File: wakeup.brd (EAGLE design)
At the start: 100 x 80 mm, 14 parts, among them IC2 ATMEGA48/88/168-AU

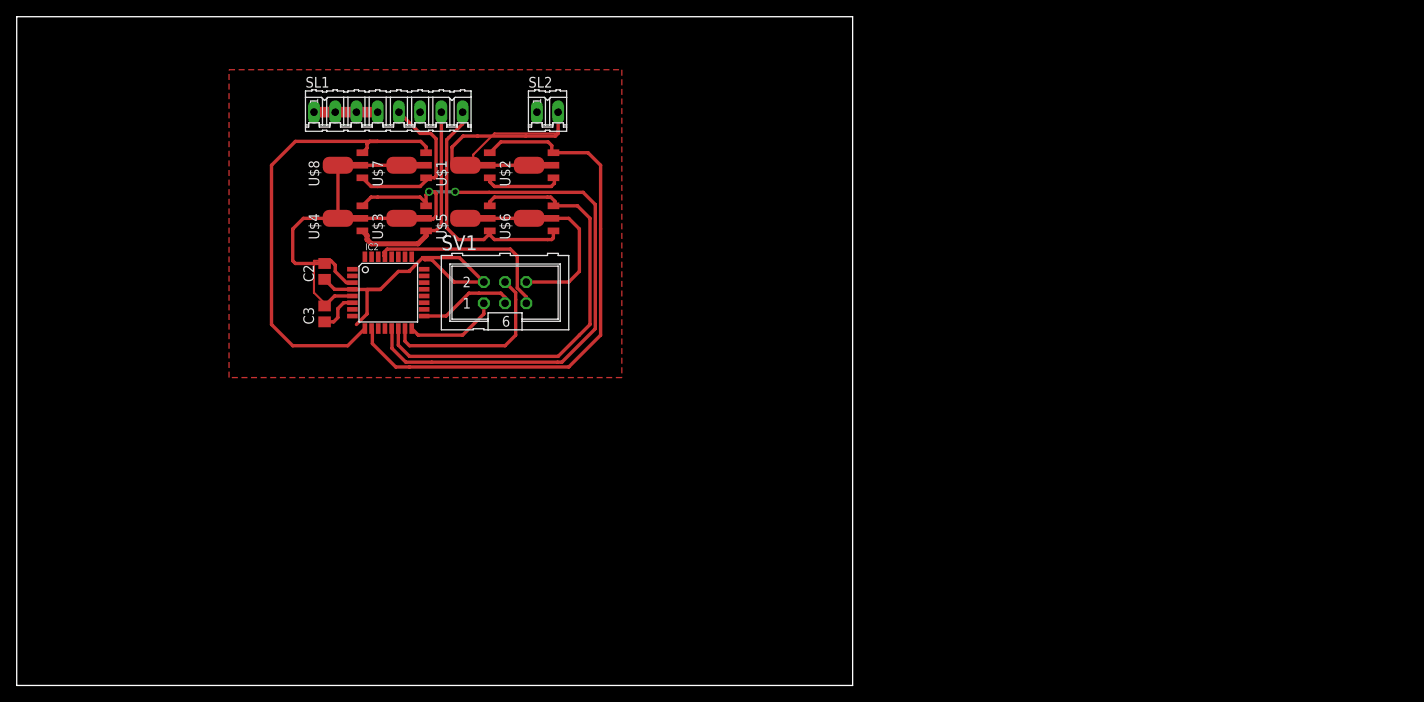
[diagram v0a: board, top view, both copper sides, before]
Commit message: Added RaspberryPi Library
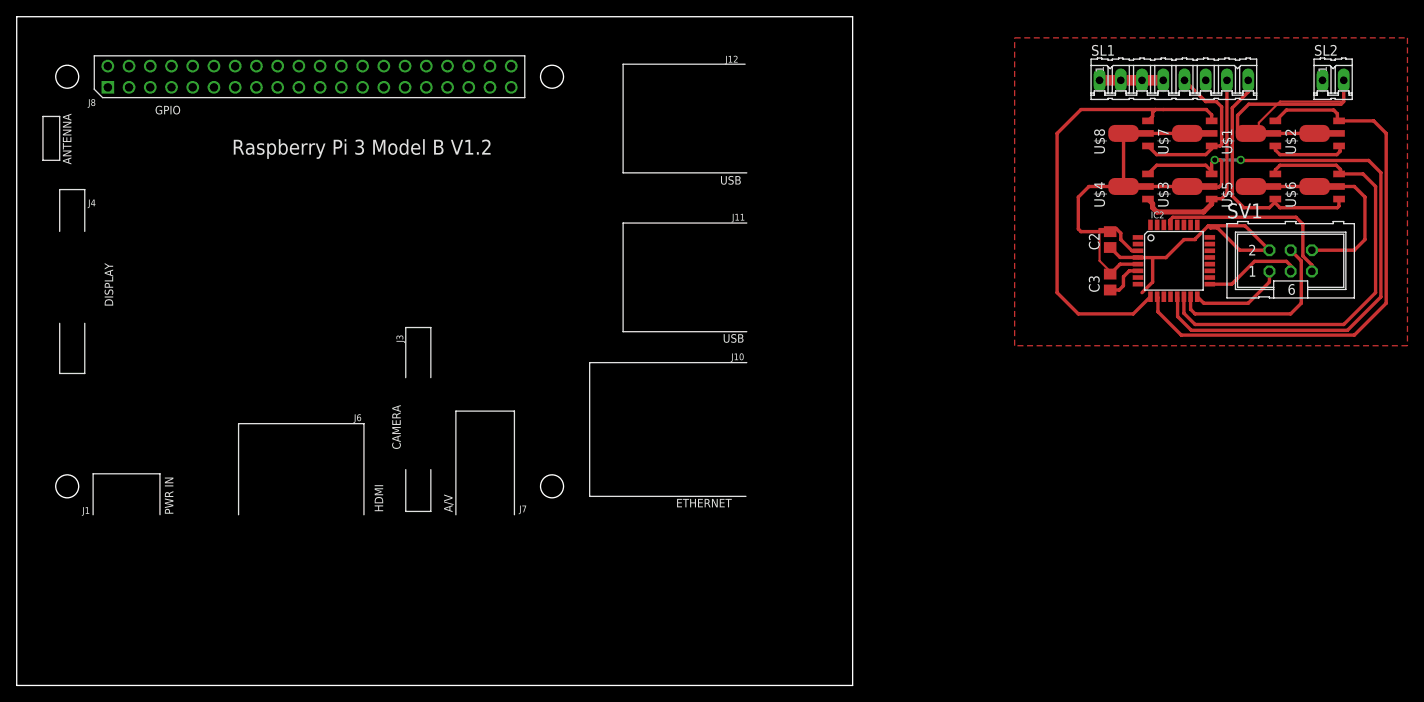
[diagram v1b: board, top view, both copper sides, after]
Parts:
- added PCB1: RPI3, e14_Rpi3_RevA:RPI3
- moved U$4 94.1 mm to (132.1, 59.7)
- moved U$8 94.1 mm to (132.1, 66.0)
- moved C2 94.1 mm to (130.8, 53.3)
- moved C3 94.1 mm to (130.8, 48.3)
- moved IC2 94.1 mm to (138.4, 50.8)
- moved SL1 94.1 mm to (138.4, 72.4)
- moved SV1 94.1 mm to (152.4, 50.8)
- moved SL2 94.1 mm to (157.5, 72.4)
- moved U$1 94.1 mm to (147.3, 66.0)
- moved U$2 94.1 mm to (154.9, 66.0)
- moved U$3 94.1 mm to (139.7, 59.7)
- moved U$5 94.1 mm to (147.3, 59.7)
- moved U$6 94.1 mm to (154.9, 59.7)
- moved U$7 94.1 mm to (139.7, 66.0)
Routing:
- net VCC: track 49.7 -> 48.1 mm
- net RED_LED: track 55.5 -> 54.5 mm
- net GND: track 130.0 -> 129.1 mm

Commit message: Updated board and schematics for RaspberryPI
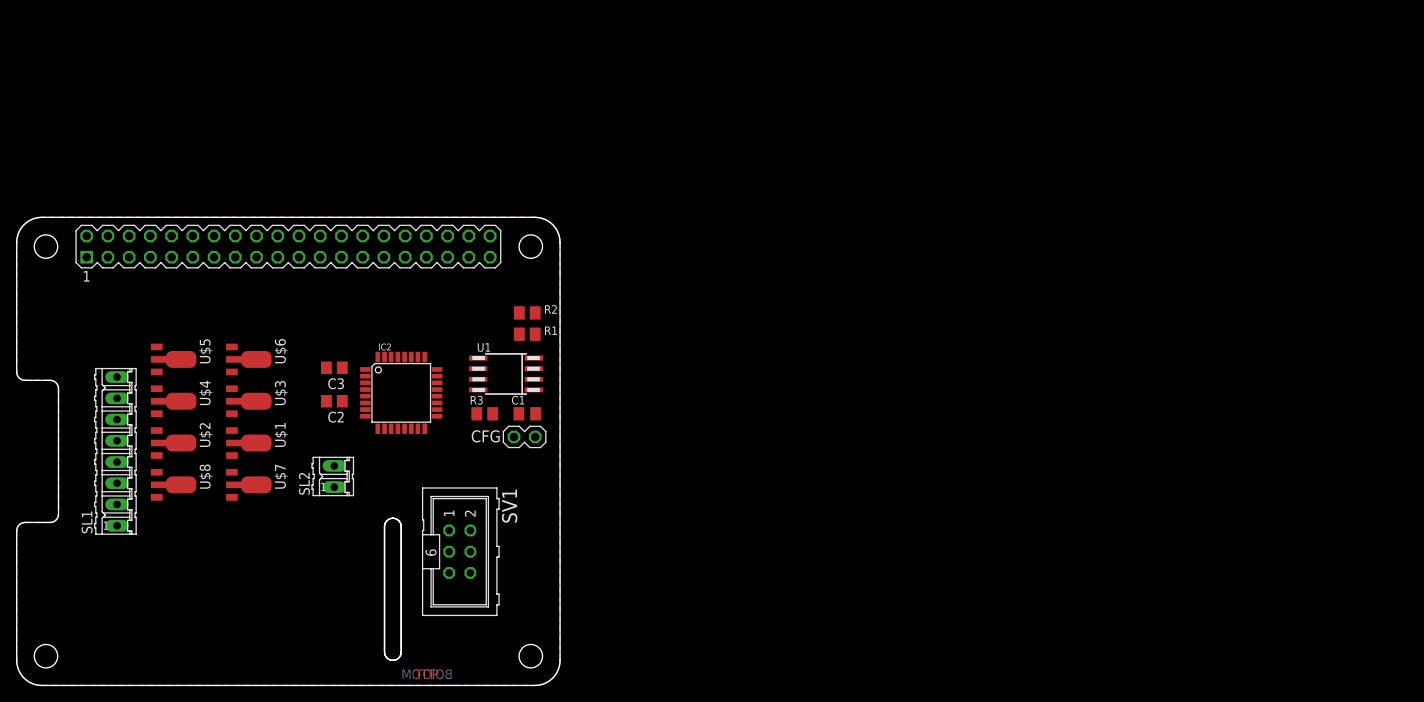
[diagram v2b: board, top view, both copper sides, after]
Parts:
- removed PCB1: RPI3, e14_Rpi3_RevA:RPI3
- added C1: 100nF, resistor:C0805K
- added CFG: (no value), FLYFISH:PIN_W_2
- added K1: PIN20X2, FLYFISH:PIN_20X2
- added R1, R2: 3k9, resistor:M0805
- added R3: 1k, resistor:M0805
- added U1: EEPROM24, FLYFISH:SOIC8
- moved U$2 139.9 mm to (20.0, 29.0), turned to 270 degrees
- moved SL1 134.0 mm to (12.0, 28.0), turned to 90 degrees
- moved U$5 129.0 mm to (20.0, 39.0), turned to 270 degrees
- moved SL2 128.5 mm to (38.0, 25.0), turned to 90 degrees
- moved U$6 127.6 mm to (29.0, 39.0), turned to 270 degrees
- moved U$1 124.0 mm to (29.0, 29.0), turned to 270 degrees
- moved U$8 119.7 mm to (20.0, 24.0), turned to 270 degrees
- moved U$7 118.4 mm to (29.0, 24.0), turned to 270 degrees
- moved U$4 115.0 mm to (20.0, 34.0), turned to 270 degrees
- moved U$3 113.6 mm to (29.0, 34.0), turned to 270 degrees
- moved SV1 105.3 mm to (53.0, 16.0), turned to 270 degrees
- moved C2 94.8 mm to (38.0, 34.0), turned to 180 degrees
- moved IC2 93.8 mm to (46.0, 35.0)
- moved C3 93.4 mm to (38.0, 38.0), turned to 180 degrees
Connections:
- new net +3V3: C1.1, K1.1, K1.17, R1.2, R2.2, R3.2, U1.8
- new net +5V: K1.2, K1.4
- new net N$1: K1.28, R1.1, U1.6
- new net N$2: K1.27, R2.1, U1.5
- new net N$3: CFG.1, R3.1, U1.7
- net GND: now also C1.2, CFG.2, K1.14, K1.20, K1.25, K1.30, K1.34, K1.39, K1.6, K1.9, U1.1, U1.2, U1.3, U1.4
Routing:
- net GND: track 129.1 -> 0.00 mm
- net BLUE_LED: track 71.3 -> 0.00 mm
- net GREEN_LED: track 67.5 -> 0.00 mm
- net RED_LED: track 54.5 -> 0.00 mm
- net WHITE_LED: track 54.1 -> 0.00 mm
- net VCC: track 48.1 -> 0.00 mm
- net WHITE_LED_OUT: track 30.2 -> 0.00 mm
- net BLUE_LED_OUT: track 25.2 -> 0.00 mm
- net RESET: track 23.1 -> 0.00 mm
- net MOSI: track 22.4 -> 0.00 mm
- net RED_LED_OUT: track 20.2 -> 0.00 mm
- net SCK: track 11.7 -> 0.00 mm
- net MISO: track 11.3 -> 0.00 mm
- net GREEN_LED_OUT: track 9.31 -> 0.00 mm
- net N$3: track 3.18 -> 0.00 mm, vias 1 -> 0
- added copper zone on layer 1, net GND
- added copper zone on layer 16, net GND
- removed copper zone on layer 1, net VCC
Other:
- board size 100 x 80 mm -> 65 x 56 mm
- board text added: "BOTTOM"
- board text added: "TOP"

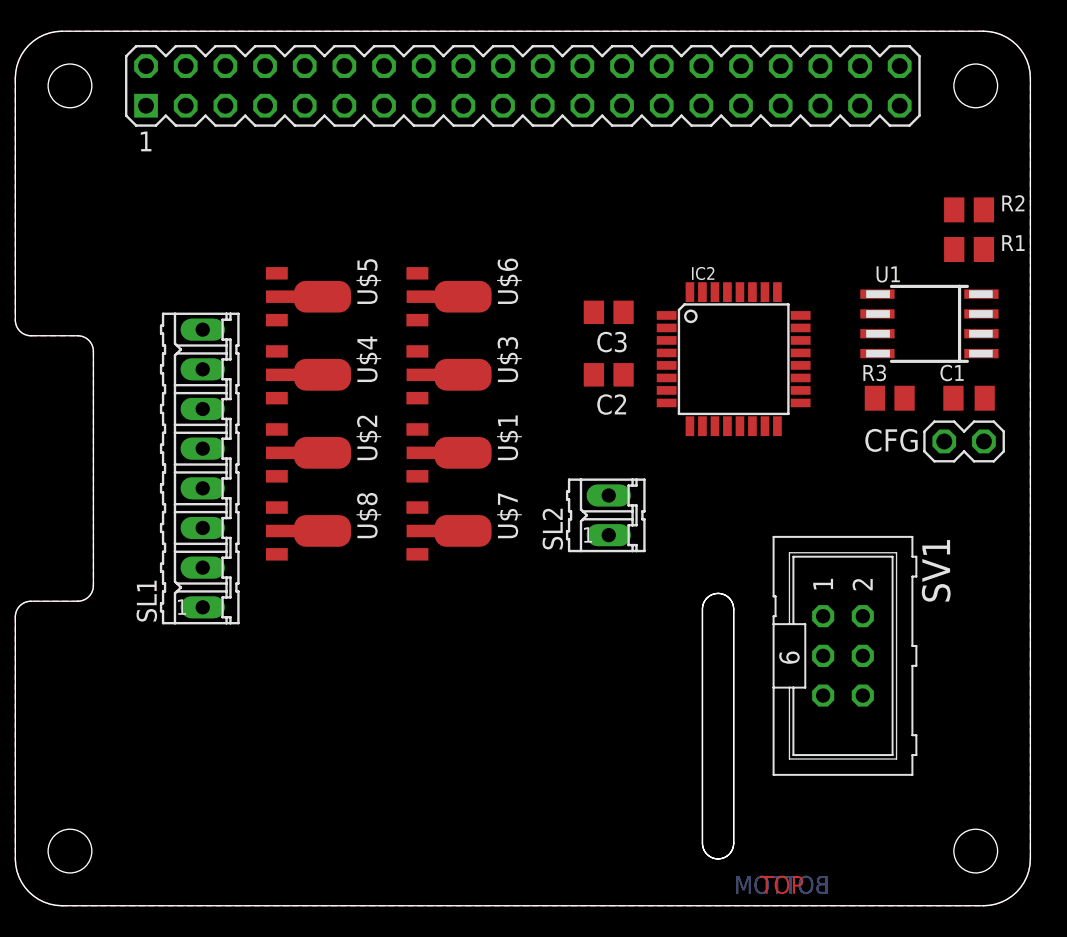
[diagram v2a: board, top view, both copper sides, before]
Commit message: Added Power connector and named some nets
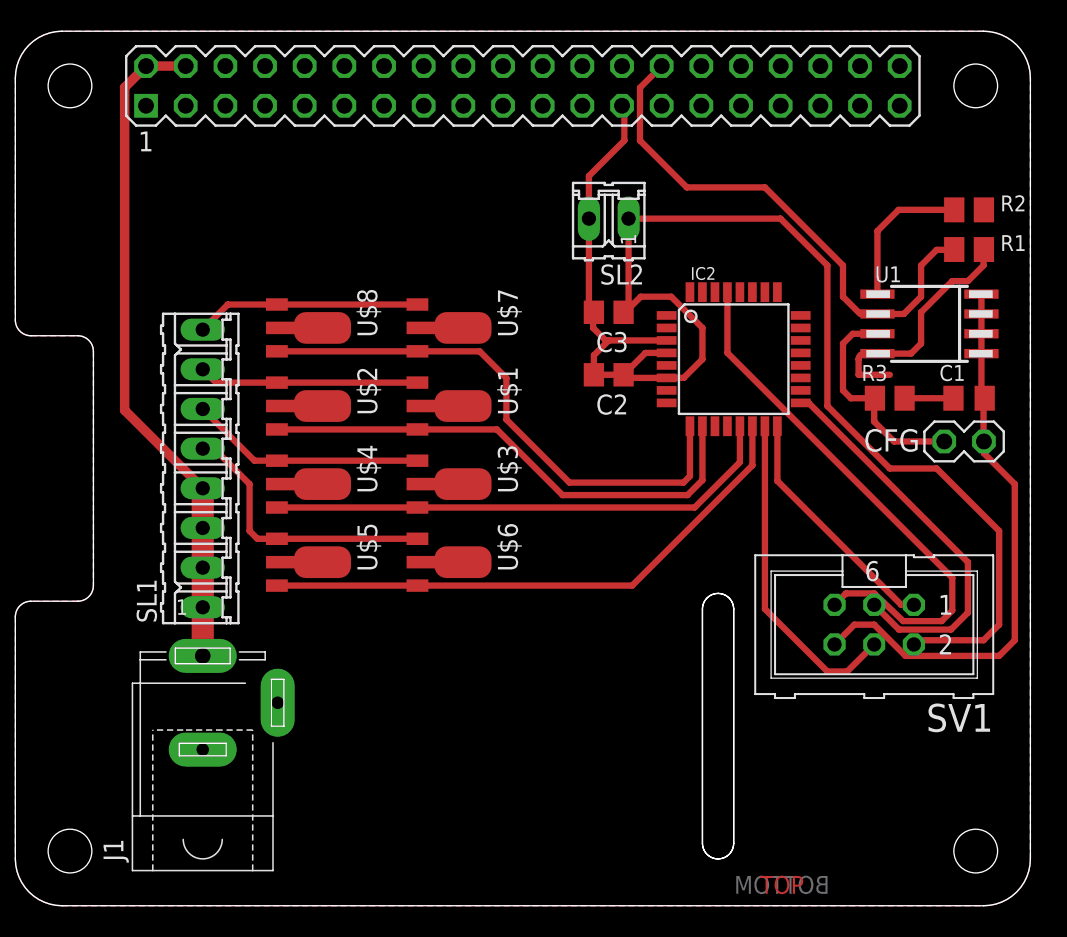
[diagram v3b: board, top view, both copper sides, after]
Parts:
- added J1: (no value), con-jack:SPC4078
- moved SL2 19.0 mm to (38.0, 44.0), turned to 180 degrees
- moved U$5 17.0 mm to (20.0, 22.0)
- moved U$6 17.0 mm to (29.0, 22.0)
- moved U$7 13.0 mm to (29.0, 37.0)
- moved U$8 13.0 mm to (20.0, 37.0)
- moved U$3 7.00 mm to (29.0, 27.0)
- moved U$4 7.00 mm to (20.0, 27.0)
- moved U$1 3.00 mm to (29.0, 32.0)
- moved U$2 3.00 mm to (20.0, 32.0)
- moved SV1 2.83 mm to (55.0, 18.0), turned to 180 degrees
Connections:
- net N$1 renamed SCL0_I2C_ID_EEPROM
- net N$2 renamed SDA0_I2C_ID_EEPROM
- new net I2C_SCL1: K1.5
- new net I2C_SDA1: K1.3
- new net MISO_SPI: K1.21
- new net MOSI_SPI: K1.19
- new net SCLK_SPI: K1.23
- net +5V: now also J1.3, SL1.1, SL1.2, SL1.3, SL1.4
- net BLUE_LED_OUT: now also SL1.6; no longer SL1.7
- net GND: now also J1.1, J1.2
- net GREEN_LED_OUT: now also SL1.7; no longer SL1.6
- net RED_LED_OUT: now also SL1.8; no longer SL1.5
- net VCC: no longer SL1.1, SL1.2, SL1.3, SL1.4
- net WHITE_LED_OUT: now also SL1.5; no longer SL1.8
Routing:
- net VCC: track 0.00 -> 75.2 mm
- net GND: track 0.00 -> 59.4 mm
- net +5V: track 0.00 -> 42.9 mm
- net WHITE_LED: track 0.00 -> 36.1 mm
- net RESET: track 0.00 -> 35.2 mm
- net RED_LED: track 0.00 -> 34.9 mm
- net BLUE_LED: track 0.00 -> 33.2 mm
- net SCL0_I2C_ID_EEPROM: track 0.00 -> 33.0 mm
- net GREEN_LED: track 0.00 -> 32.8 mm
- net SCK: track 0.00 -> 25.3 mm
- net MOSI: track 0.00 -> 21.1 mm
- net +3V3: track 0.00 -> 18.8 mm
- net WHITE_LED_OUT: track 0.00 -> 17.9 mm
- net MISO: track 0.00 -> 15.5 mm
- net BLUE_LED_OUT: track 0.00 -> 15.1 mm
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
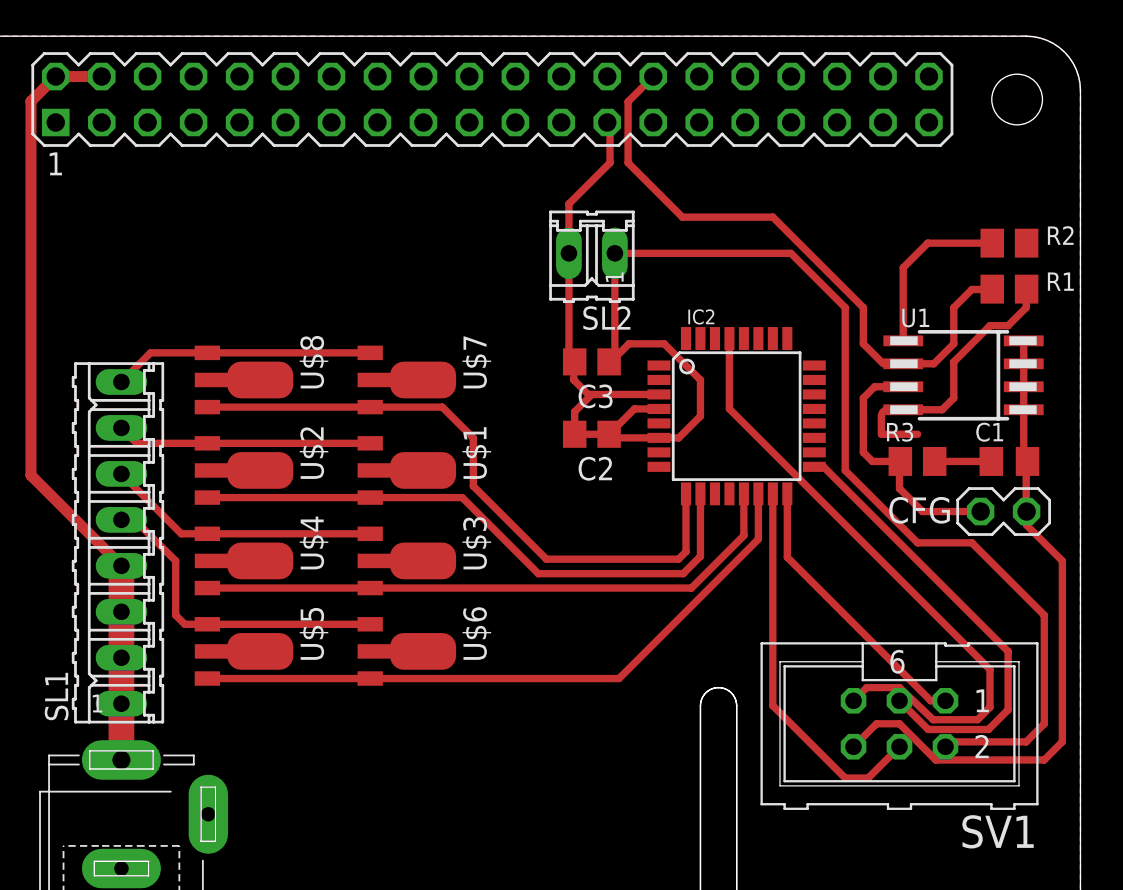
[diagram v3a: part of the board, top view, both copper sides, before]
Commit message: Updated layout
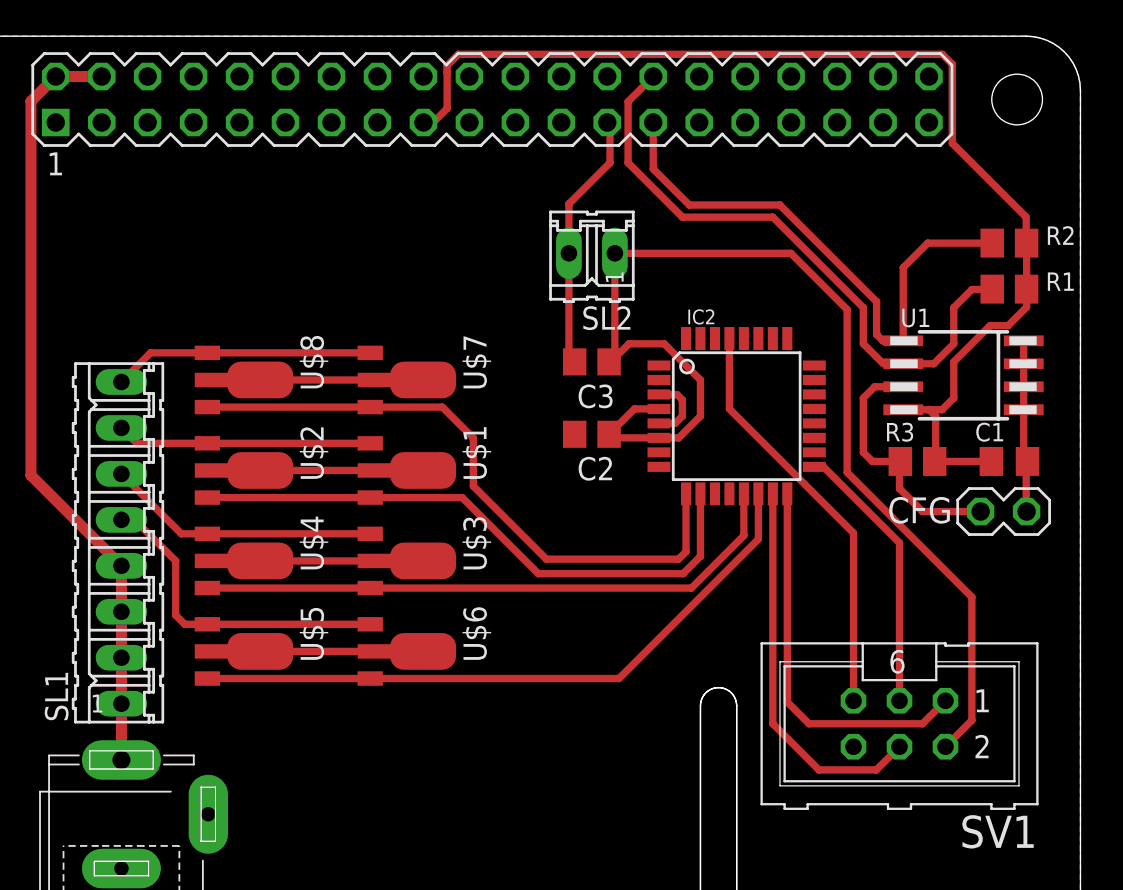
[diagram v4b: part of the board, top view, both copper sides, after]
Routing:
- net +3V3: track 18.8 -> 64.0 mm
- net SDA0_I2C_ID_EEPROM: track 9.52 -> 30.9 mm
- net RESET: track 35.2 -> 22.9 mm
- net SCK: track 25.3 -> 15.2 mm
- net VCC: track 75.2 -> 65.2 mm
- net MISO: track 15.5 -> 21.3 mm
- net GND: track 59.4 -> 53.7 mm
